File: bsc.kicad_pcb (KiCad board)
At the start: 4 copper layers, 120 x 100 mm, 286 parts, among them IC1 ILD217T, IC2 ILD217T, IC3 ILD217T, J1 Conn_JTAG_ESP, J10 JP_REL1_COM_12V, J12 JP_REL2_COM_12V, J13 JP_REL3_COM_12V, J14 Conn_REL1, J15 Conn_REL2, J16 Conn_REL3, J2 Prog, J3 Conn_Extension, J4 Boot, J5 JP_REL4_COM_12V, J6 JP_U3TX_EN, J8 JP_REL5_COM_12V, J9 JP_REL6_COM_12V, K2 TIANBO-HJR-4102-L, K3 TIANBO-HJR-4102-L, K4 TIANBO-HJR-4102-L, K5 TIANBO-HJR-4102-L, K6 TIANBO-HJR-4102-L, K7 TIANBO-HJR-4102-L, Q1 BC857BS, Q10 BC846, Q11 BC846, Q12 IRLML2244, Q13 BC857BS, Q14 IRLML2244, Q15 BSS138, Q2 BSS138, Q3 BSS138, Q4 BSS138, Q5 BSS138, Q6 BSS138, Q7 BSS138, Q8 BC846, Q9 BC846, U1 K7803-1000R3, U10 74HC595, U11 74HC14, U12 74HC165, U13 ADuM1201AR, U16 SP3485EN, U19 LMO78_05-0.5, U2 ESP32WROOM32E16, U20 HC 151, U3 ADM2483xRW, U4 ADuM1201AR, U6 ADuM1201AR, U7 SN65HVD234, U8 SP3485EN, X1 Conn_S2, X2 Conn_S1, X3 Conn_DI, X4 Conn_SV, X5 Conn_Rel2, X6 Conn_Rel1

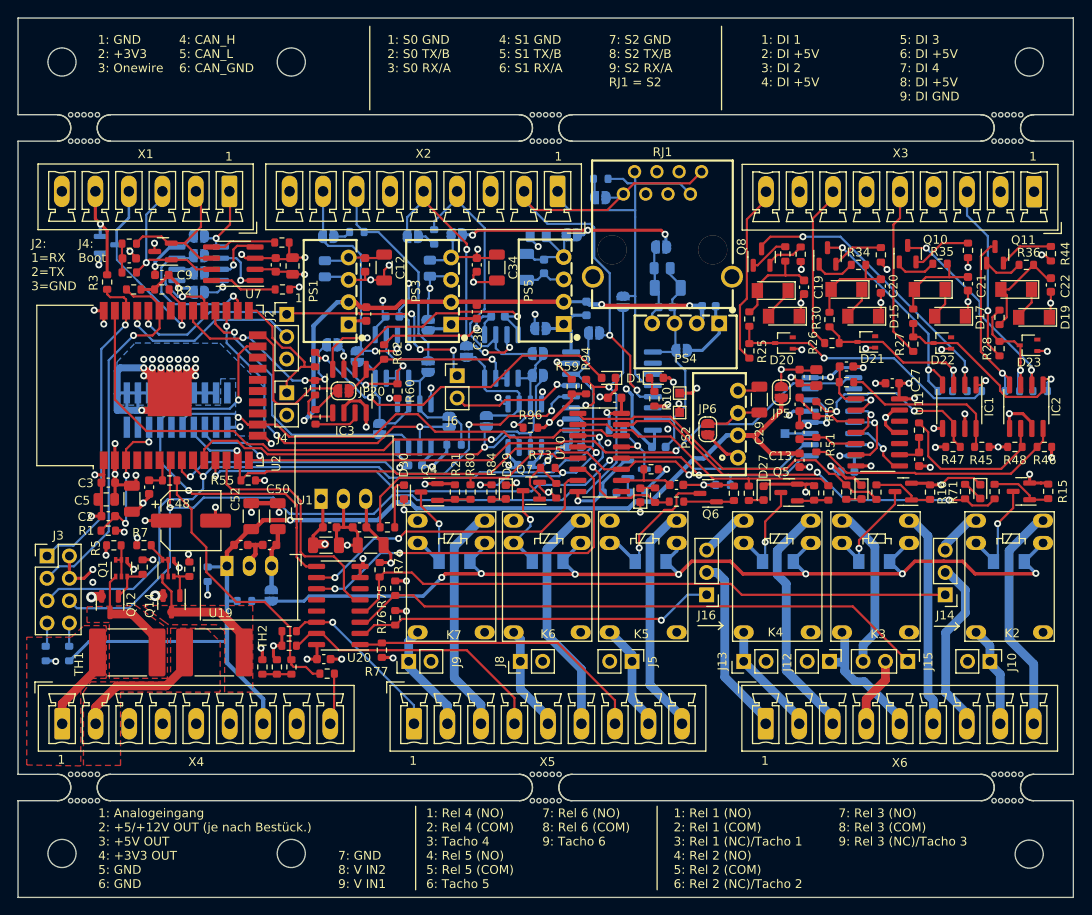
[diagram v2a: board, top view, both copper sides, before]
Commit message: Slikscreen changed
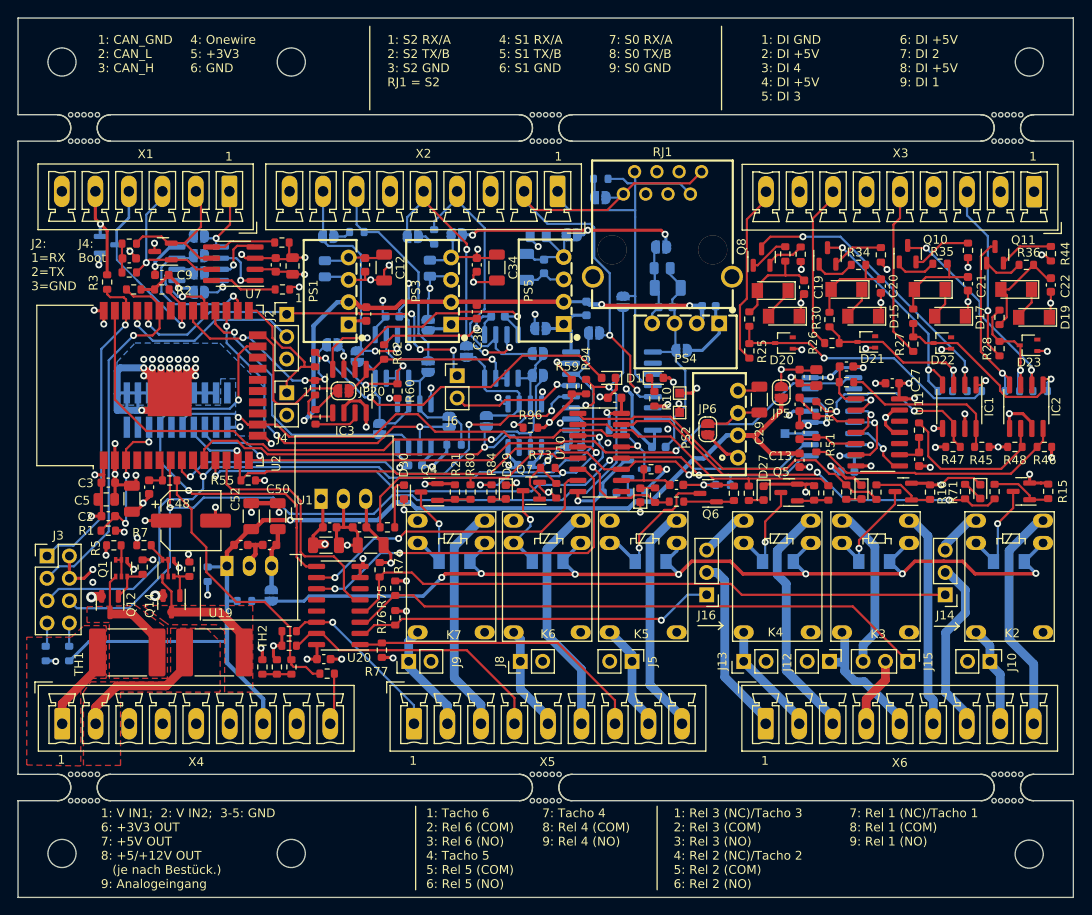
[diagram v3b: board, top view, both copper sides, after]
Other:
- board text added: "1: CAN_GND 2: CAN_L 3: CAN_H"
- board text added: "1: DI GND 2: DI +5V 3: DI 4 4: DI +5V 5: DI 3"
- board text added: "1: Rel 3 (NC)/Tacho 3 2: Rel 3 (COM) 3: Rel 3 (NO) 4: Rel 2 (NC)/Tacho 2 5: Rel 2 (COM) 6: Rel 2 (NO)"
- board text added: "1: S2 RX/A 2: S2 TX/B 3: S2 GND RJ1 = S2"
- board text added: "1: Tacho 6 2: Rel 6 (COM) 3: Rel 6 (NO) 4: Tacho 5 5: Rel 5 (COM) 6: Rel 5 (NO)"
- board text added: "1: V IN1; 2: V IN2; 3-5: GND 6: +3V3 OUT 7: +5V OUT 8: +5/+12V OUT (je nach Bestück.) 9: Analogeingang"
- board text added: "4: Onewire 5: +3V3 6: GND"
- board text added: "4: S1 RX/A 5: S1 TX/B 6: S1 GND"
- board text added: "6: DI +5V 7: DI 2 8: DI +5V 9: DI 1"
- board text added: "7: Rel 1 (NC)/Tacho 1 8: Rel 1 (COM) 9: Rel 1 (NO)"
- board text added: "7: S0 RX/A 8: S0 TX/B 9: S0 GND"
- board text added: "7: Tacho 4 8: Rel 4 (COM) 9: Rel 4 (NO)"
- board text removed: "1: Analogeingang 2: +5/+12V OUT (je nach Bestück.) 3: +5V OUT 4: +3V3 OUT 5: GND 6: GND"
- board text removed: "1: DI 1 2: DI +5V 3: DI 2 4: DI +5V"
- board text removed: "1: GND 2: +3V3 3: Onewire"
- board text removed: "1: Rel 1 (NO) 2: Rel 1 (COM) 3: Rel 1 (NC)/Tacho 1 4: Rel 2 (NO) 5: Rel 2 (COM) 6: Rel 2 (NC)/Tacho 2"
- board text removed: "1: Rel 4 (NO) 2: Rel 4 (COM) 3: Tacho 4 4: Rel 5 (NO) 5: Rel 5 (COM) 6: Tacho 5"
- board text removed: "1: S0 GND 2: S0 TX/B 3: S0 RX/A"
- board text removed: "4: CAN_H 5: CAN_L 6: CAN_GND"
- board text removed: "4: S1 GND 5: S1 TX/B 6: S1 RX/A"
- board text removed: "5: DI 3 6: DI +5V 7: DI 4 8: DI +5V 9: DI GND"
- board text removed: "7: GND 8: V IN2 9: V IN1"
- board text removed: "7: Rel 3 (NO) 8: Rel 3 (COM) 9: Rel 3 (NC)/Tacho 3"
- board text removed: "7: Rel 6 (NO) 8: Rel 6 (COM) 9: Tacho 6"
- board text removed: "7: S2 GND 8: S2 TX/B 9: S2 RX/A RJ1 = S2"
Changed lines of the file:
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@@
     (effects (font (size 1 1) (thickness 0.15)) (justify left mirror))
   )
-  (gr_text "1: Rel 1 (NO)\n2: Rel 1 (COM)\n3: Rel 1 (NC)/Tacho 1\n4: Rel 2 (NO)\n5: Rel 2 (COM)\n6: Rel 2 (NC)/Tacho 2\n" (at 104.5464 110.4392) (layer "F.SilkS")
+  (gr_text "1: Rel 3 (NC)/Tacho 3\n2: Rel 3 (COM)\n3: Rel 3 (NO)\n4: Rel 2 (NC)/Tacho 2\n5: Rel 2 (COM)\n6: Rel 2 (NO)" (at 104.5464 110.4392) (layer "F.SilkS")
     (effects (font (size 1 1) (thickness 0.15)) (justify left))
   )
@@
     (effects (font (size 1 1) (thickness 0.15)))
   )
-  (gr_text "1: S0 GND\n2: S0 TX/B\n3: S0 RX/A" (at 71.9836 20.0816) (layer "F.SilkS")
+  (gr_text "1: S2 RX/A\n2: S2 TX/B\n3: S2 GND\nRJ1 = S2" (at 71.9836 20.8866) (layer "F.SilkS")
     (effects (font (size 1 1) (thickness 0.15)) (justify left))
   )
-  (gr_text "4: CAN_H\n5: CAN_L\n6: CAN_GND" (at 48.3108 20.0816) (layer "F.SilkS")
+  (gr_text "4: Onewire\n5: +3V3\n6: GND" (at 49.5808 20.0816) (layer "F.SilkS")
     (effects (font (size 1 1) (thickness 0.15)) (justify left))
   )
@@
     (effects (font (size 1 1) (thickness 0.15)) (justify left))
   )
-  (gr_text "1: DI 1\n2: DI +5V\n3: DI 2\n4: DI +5V\n" (at 114.5 20.8866) (layer "F.SilkS")
+  (gr_text "1: DI GND\n2: DI +5V\n3: DI 4\n4: DI +5V\n5: DI 3" (at 114.5 21.6916) (layer "F.SilkS")
     (effects (font (size 1 1) (thickness 0.15)) (justify left))
   )
-  (gr_text "1: Analogeingang\n2: +5/+12V OUT (je nach Bestück.)\n3: +5V OUT\n4: +3V3 OUT\n5: GND\n6: GND" (at 39.116 110.4392) (layer "F.SilkS")
+  (gr_text "1: V IN1;  2: V IN2;  3-5: GND\n6: +3V3 OUT\n7: +5V OUT\n8: +5/+12V OUT \n   (je nach Bestück.)\n9: Analogeingang" (at 39.4208 110.4392) (layer "F.SilkS")
     (effects (font (size 1 1) (thickness 0.15)) (justify left))
   )
@@
     (effects (font (size 1 1) (thickness 0.15)) (justify left))
   )
-  (gr_text "5: DI 3\n6: DI +5V\n7: DI 4\n8: DI +5V\n9: DI GND" (at 130.2512 21.6916) (layer "F.SilkS")
+  (gr_text "6: DI +5V\n7: DI 2\n8: DI +5V\n9: DI 1" (at 130.2512 20.8866) (layer "F.SilkS")
     (effects (font (size 1 1) (thickness 0.15)) (justify left))
   )
-  (gr_text "4: S1 GND\n5: S1 TX/B\n6: S1 RX/A" (at 84.6836 20.0816) (layer "F.SilkS")
+  (gr_text "4: S1 RX/A\n5: S1 TX/B\n6: S1 GND" (at 84.6836 20.0816) (layer "F.SilkS")
     (effects (font (size 1 1) (thickness 0.15)) (justify left))
   )
@@
     (effects (font (size 1 1) (thickness 0.15)))
   )
-  (gr_text "7: S2 GND\n8: S2 TX/B\n9: S2 RX/A\nRJ1 = S2" (at 97.1804 20.8866) (layer "F.SilkS")
+  (gr_text "7: S0 RX/A\n8: S0 TX/B\n9: S0 GND" (at 97.1804 20.0816) (layer "F.SilkS")
     (effects (font (size 1 1) (thickness 0.15)) (justify left))
   )
-  (gr_text "1: Rel 4 (NO)\n2: Rel 4 (COM)\n3: Tacho 4\n4: Rel 5 (NO)\n5: Rel 5 (COM)\n6: Tacho 5" (at 76.4032 110.4392) (layer "F.SilkS")
+  (gr_text "1: Tacho 6\n2: Rel 6 (COM)\n3: Rel 6 (NO)\n4: Tacho 5\n5: Rel 5 (COM)\n6: Rel 5 (NO)" (at 76.4032 110.4392) (layer "F.SilkS")
     (effects (font (size 1 1) (thickness 0.15)) (justify left))
   )
@@
     (effects (font (size 1 1) (thickness 0.15)))
   )
-  (gr_text "1: GND\n2: +3V3\n3: Onewire" (at 39.0652 20.0816) (layer "F.SilkS")
+  (gr_text "1: CAN_GND\n2: CAN_L\n3: CAN_H" (at 39.0652 20.0816) (layer "F.SilkS")
     (effects (font (size 1 1) (thickness 0.15)) (justify left))
   )
-  (gr_text "7: Rel 3 (NO)\n8: Rel 3 (COM)\n9: Rel 3 (NC)/Tacho 3" (at 123.2916 108.0242) (layer "F.SilkS")
+  (gr_text "7: Rel 1 (NC)/Tacho 1\n8: Rel 1 (COM)\n9: Rel 1 (NO)" (at 124.5362 108.0242) (layer "F.SilkS")
     (effects (font (size 1 1) (thickness 0.15)) (justify left))
   )
@@
     (effects (font (size 1 1) (thickness 0.15)))
   )
-  (gr_text "7: Rel 6 (NO)\n8: Rel 6 (COM)\n9: Tacho 6" (at 89.6112 108.0242) (layer "F.SilkS")
+  (gr_text "7: Tacho 4\n8: Rel 4 (COM)\n9: Rel 4 (NO)" (at 89.6112 108.0242) (layer "F.SilkS")
     (effects (font (size 1 1) (thickness 0.15)) (justify left))
   )
@@
     (effects (font (size 1 1) (thickness 0.15)))
   )
-  (gr_text "\n7: GND\n8: V IN2\n9: V IN1" (at 66.3956 112.0492) (layer "F.SilkS")
-    (effects (font (size 1 1) (thickness 0.15)) (justify left))
-  )
   (segment (start 56.3732 74.119) (end 56.515 74.119) (width 0.5) (layer "F.Cu") (net 1))

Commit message: Fix pullup
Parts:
- moved R23 7.83 mm to (103.2, 68.8), turned to -90 degrees
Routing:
- net +3V3: track 188.2 -> 190.0 mm
- net +5V: track 194.8 -> 195.9 mm

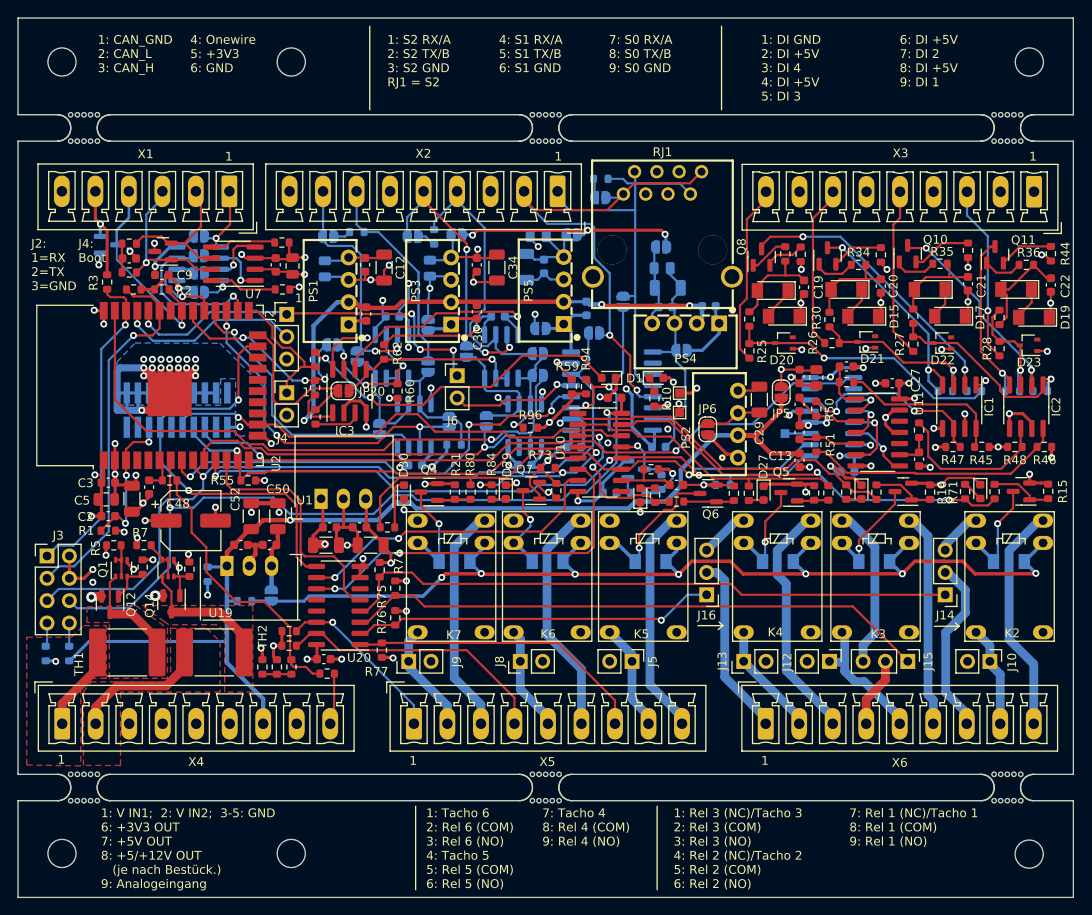
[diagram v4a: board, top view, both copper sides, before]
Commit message: RX Pullups von U1+U2 geändert
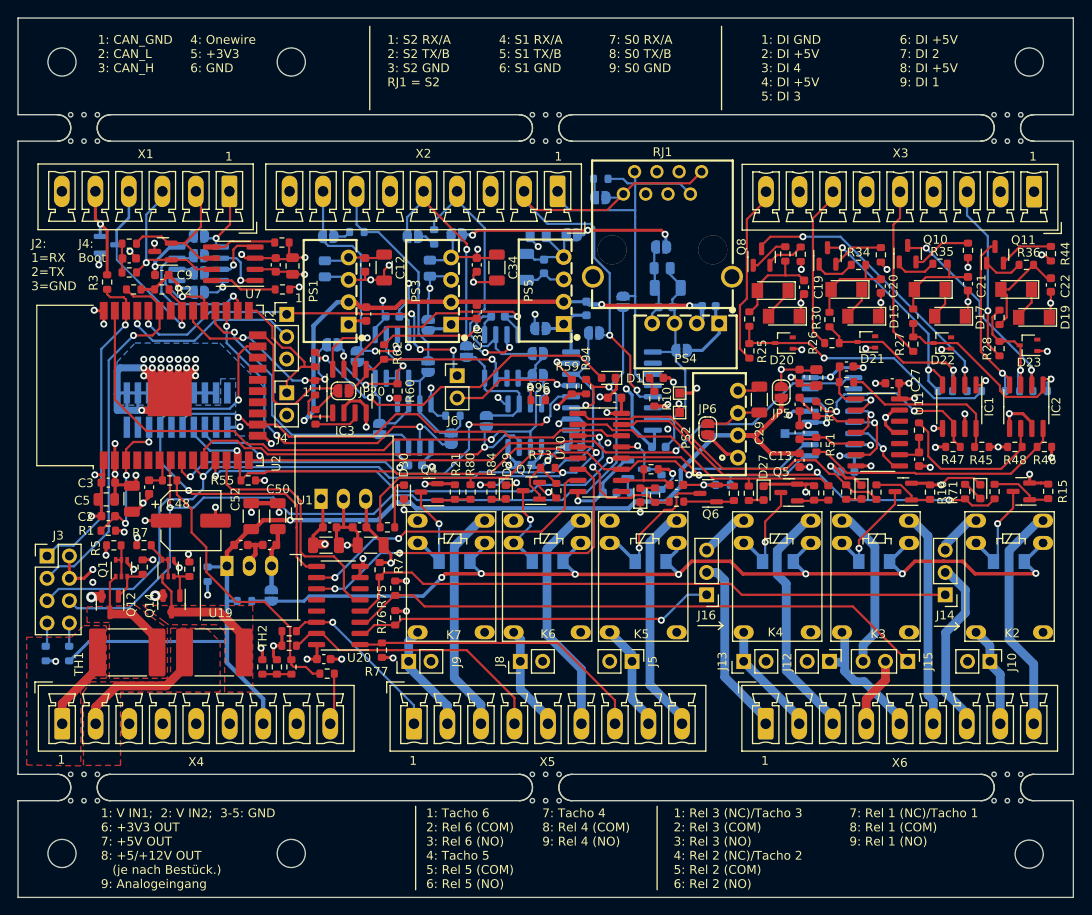
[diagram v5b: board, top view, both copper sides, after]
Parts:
- moved R95 3.30 mm to (79.5, 61.2)
- moved R96 3.25 mm to (89.2, 59.5)
- moved JP9 1.92 mm to (79.2, 63.8)
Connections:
- R95 pad 2: +3V3 -> /serial/U1_VCC
- R96 pad 2: +3V3 -> /serial/U2_VCC
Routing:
- net +3V3: track 190.0 -> 181.1 mm
- net /serial/U2RX_S: track 12.1 -> 8.94 mm
- net /serial/U1_VCC: track 29.4 -> 32.0 mm
- net /serial/U2_VCC: track 38.3 -> 39.7 mm
- net /U1RX: track 39.6 -> 40.7 mm
